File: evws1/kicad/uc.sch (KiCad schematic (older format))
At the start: 78 parts, among them J13 atmega-isp-6, J14 header, J15 header, M5 rpi-ev-plc-adapter-v1.0, Q3 AO3400, SW3 SW_Push, SW4 dip-switch-4x2pos-smd-1.27mm, SW5 SS-12D00G3, SW8 dip-switch-4x2pos-smd-1.27mm, T5 header, T6 header, U1 atmega324p-20au, U4 PCF8591, U7 DS1307ZN, U8 24LC512, U9 PCF8574, Y1 20MHz, Y4 32768kHz

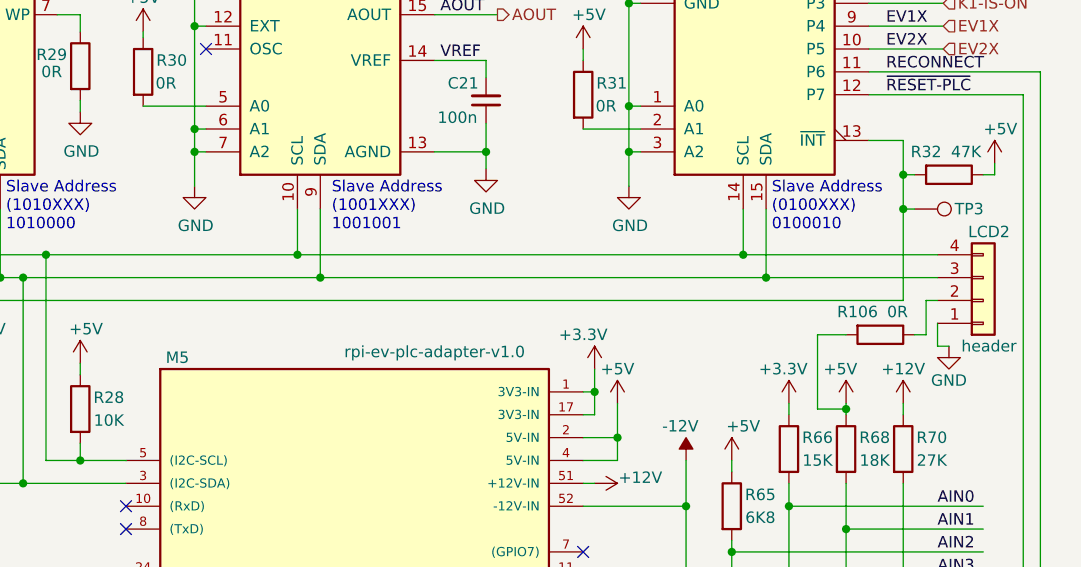
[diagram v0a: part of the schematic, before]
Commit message: fixing project problems, cause by renaming directory
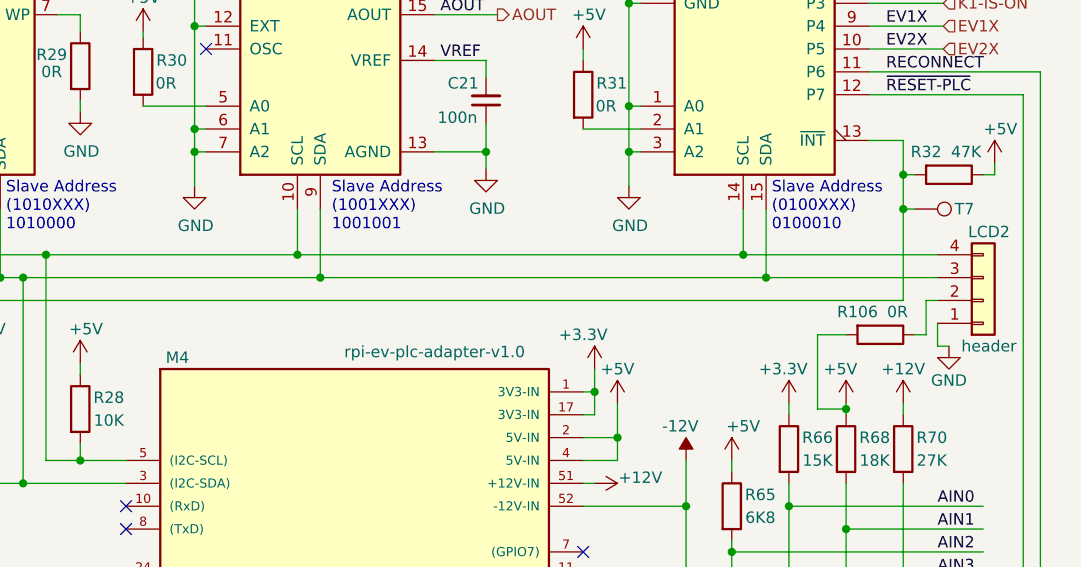
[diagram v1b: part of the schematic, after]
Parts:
- renumbered M5 to M4, TP3 to T7
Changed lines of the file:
@@
 $EndComp
 $Comp
-L _project:rpi-ev-plc-adapter-v1.0 M5
+L _project:rpi-ev-plc-adapter-v1.0 M4
 U 1 1 5E152A84
 P 8100 4600
-F 0 "M5" H 7325 6500 50  0000 C CNN
+F 0 "M4" H 7325 6500 50  0000 C CNN
 F 1 "rpi-ev-plc-adapter-v1.0" H 8450 6525 50  0000 C CNN
 F 2 "Project:rpi-ev-plc-adapter-v1.0" H 8100 4650 50  0001 C CIN
@@
 P 10550 2050
 AR Path="/5E901354" Ref="TP?"  Part="1"
-AR Path="/5E0A3961/5E901354" Ref="TP3"  Part="1"
-F 0 "TP3" V 10550 2225 50  0000 L CNN
+AR Path="/5E0A3961/5E901354" Ref="T7"  Part="1"
+F 0 "T7" V 10550 2225 50  0000 L CNN
 F 1 "TestPoint" H 10608 2079 50  0001 L CNN
 F 2 "Measurement_Points:Measurement_Point_Round-TH_Small" H 10750 2050 50  0001 C CNN
